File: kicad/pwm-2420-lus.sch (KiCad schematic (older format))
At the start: 6 parts

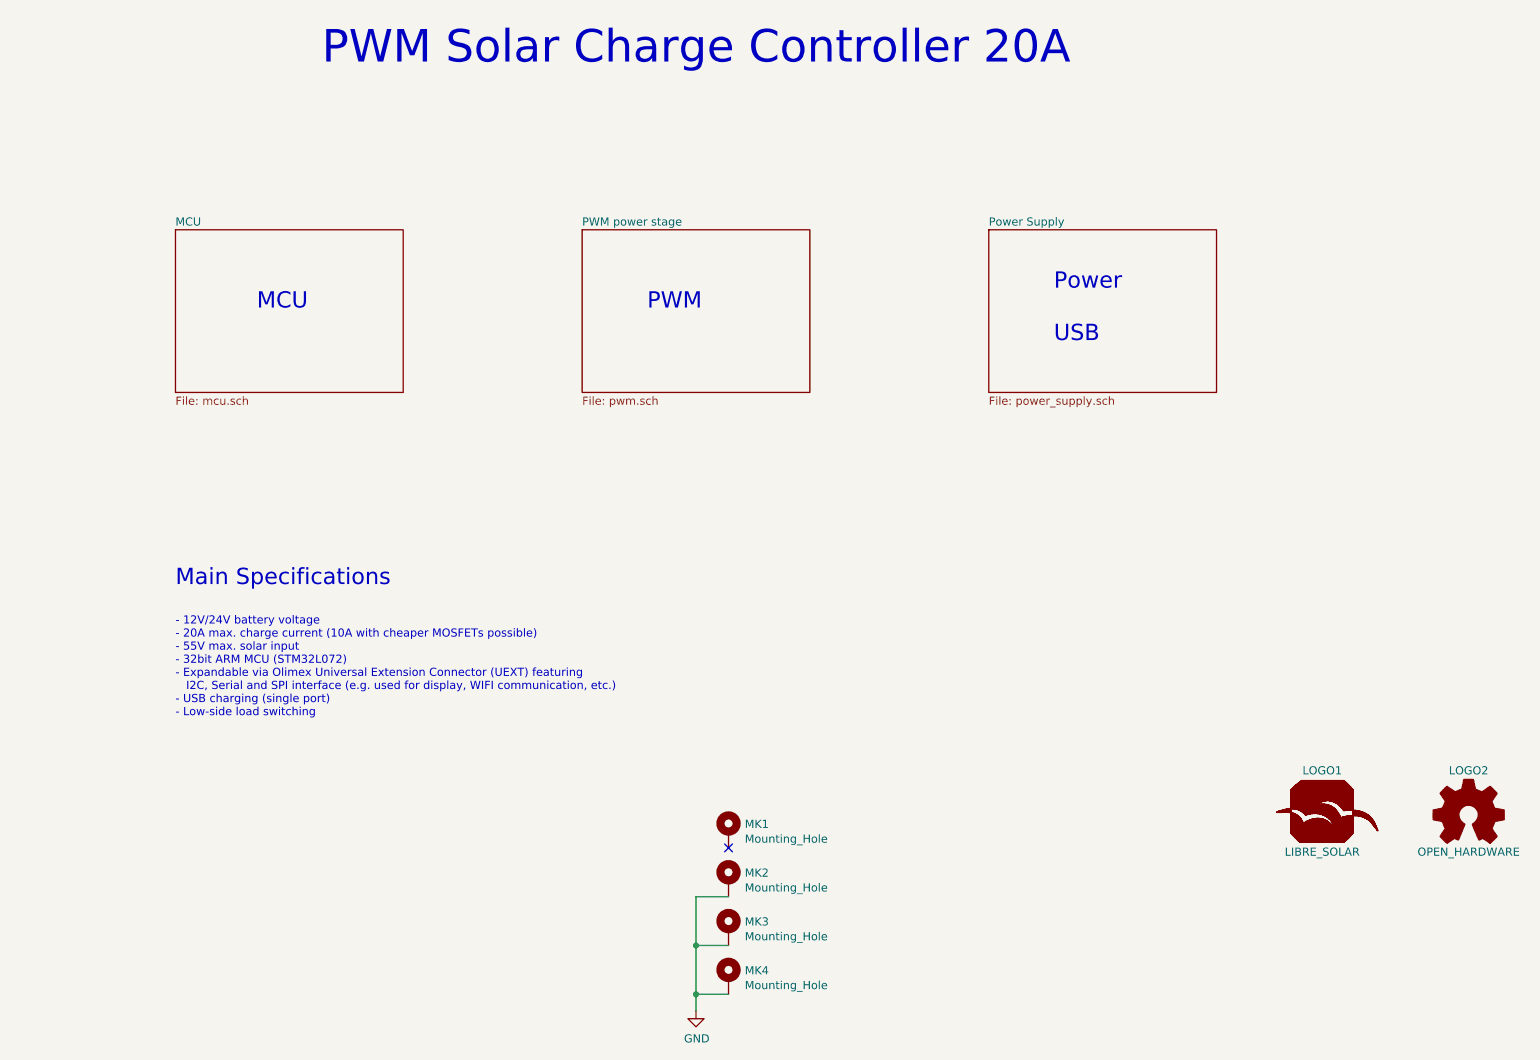
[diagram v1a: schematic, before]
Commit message: Improved power supply and exposed BOOT0 pin
- BOOT0 pin connected to BUTTON wire to allow firmware upgrade via LS.one port
- Additional emitter follower for 3V3 power supply to increase margin to 30V absolute max. rating of LDO in case of 24V battery
- Corners adjusted to match shape of MPPT 1210 HUS
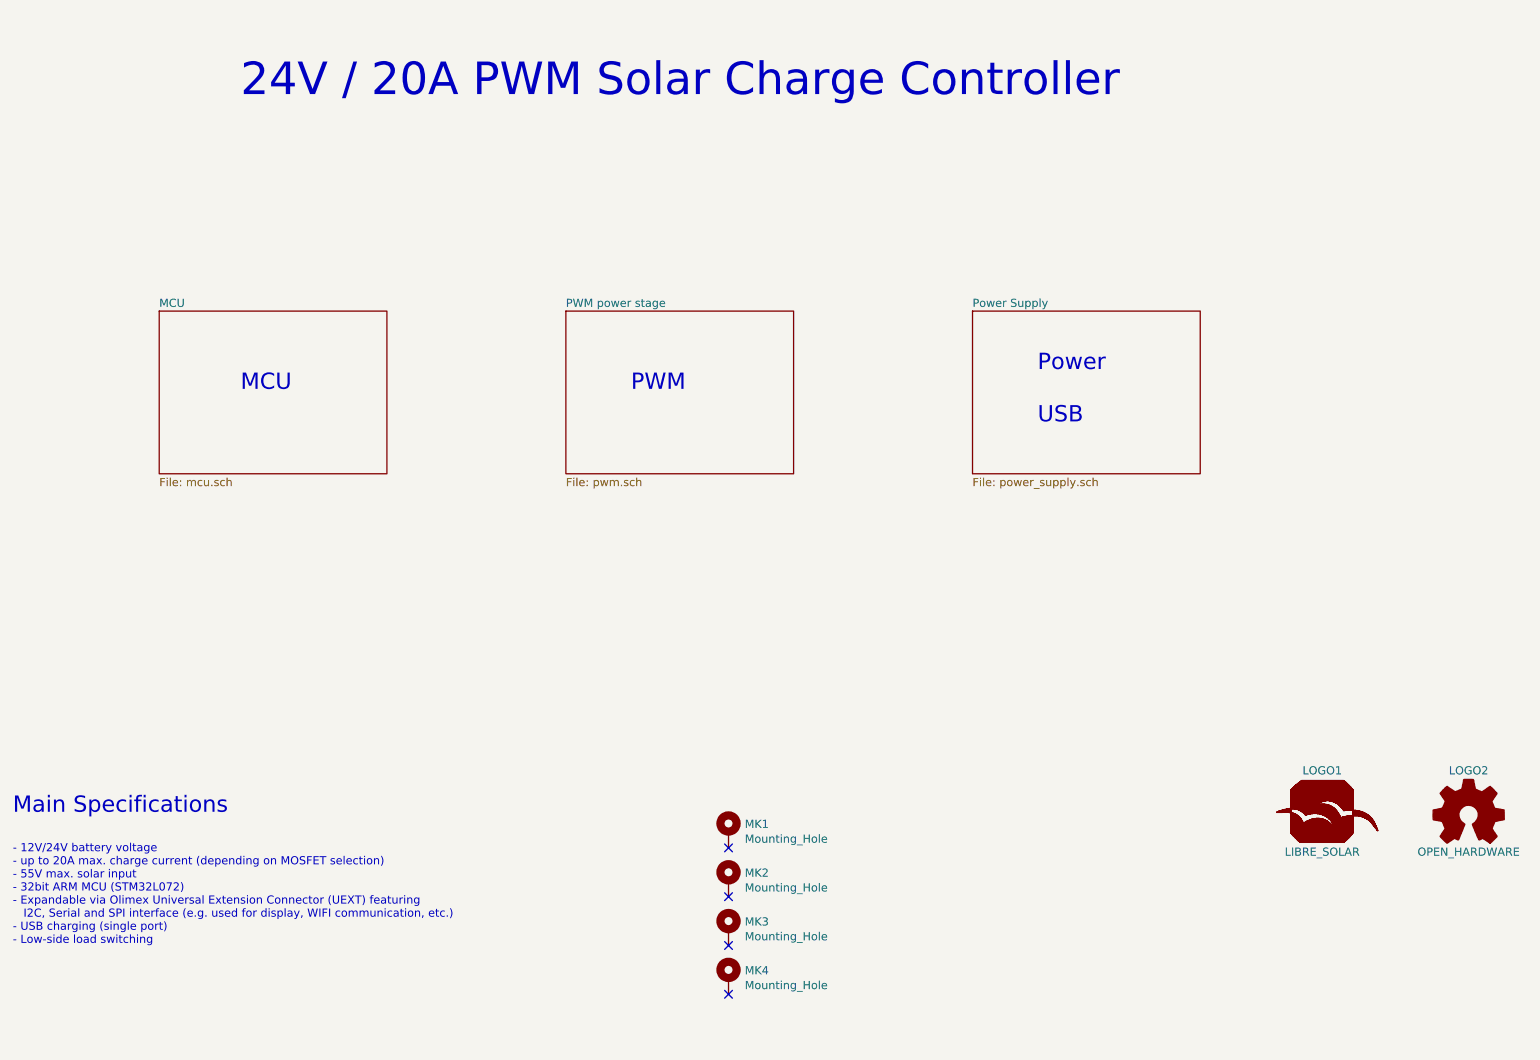
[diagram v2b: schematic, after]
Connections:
- removed net GND: MK2.1, MK3.1, MK4.1
- no-connect marks 1 -> 4
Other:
- note added: "- 12V/24V battery voltage\n- up to 20A max. charge current (depending on MOSFET selection)\n- 55V max. solar input\n- 32bit ARM MCU (STM32L072)\n- Expandable via Olimex Universal Extension Connector (UEXT) featuring\n I2C, Serial and SPI interface (e.g. used for display, WIFI communication, etc.)\n- USB charging (single port)\n- Low-side load switching\n"
- note added: "24V / 20A PWM Solar Charge Controller"
- note removed: "- 12V/24V battery voltage\n- 20A max. charge current (10A with cheaper MOSFETs possible)\n- 55V max. solar input\n- 32bit ARM MCU (STM32L072)\n- Expandable via Olimex Universal Extension Connector (UEXT) featuring\n I2C, Serial and SPI interface (e.g. used for display, WIFI communication, etc.)\n- USB charging (single port)\n- Low-side load switching\n"
- note removed: "PWM Solar Charge Controller 20A"
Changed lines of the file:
@@
 encoding utf-8
 Sheet 1 4
-Title "PWM Solar Charge Controller"
-Date "2019-04-25"
-Rev "0.2.2"
+Title "PWM 2420 LUS"
+Date "2019-08-26"
+Rev "0.3"
 Comp "Libre Solar"
 Comment1 "Author: Martin Jäger"
@@
 $EndDescr
 $Sheet
-S 5100 2500 1400 1000
+S 5000 3000 1400 1000
 U 58A68DC9
 F0 "PWM power stage" 50
@@
 $EndSheet
 $Sheet
-S 2600 2500 1400 1000
+S 2500 3000 1400 1000
 U 58A68DCB
 F0 "MCU" 50
@@
 $EndSheet
 $Sheet
-S 7600 2500 1400 1000
+S 7500 3000 1400 1000
 U 58C18D5C
 F0 "Power Supply" 50
 F1 "power_supply.sch" 50
 $EndSheet
-Text Notes 3500 1500 0    200  ~ 0
-PWM Solar Charge Controller 20A
-Text Notes 2600 4700 0    100  ~ 0
+Text Notes 3000 1700 0    200  ~ 0
+24V / 20A PWM Solar Charge Controller
+Text Notes 1600 6100 0    100  ~ 0
 Main Specifications
-Text Notes 2600 5500 0    50   ~ 0
-- 12V/24V battery voltage\n- 20A max. charge current (10A with cheaper MOSFETs possible)\n- 55V max. solar input\n- 32bit ARM MCU (STM32L072)\n- Expandable via Olimex Universal Extension Connector (UEXT) featuring\n   I2C, Serial and SPI interface (e.g. used for display, WIFI communication, etc.)\n- USB charging (single port)\n- Low-side load switching\n
+Text Notes 1600 6900 0    50   ~ 0
+- 12V/24V battery voltage\n- up to 20A max. charge current (depending on MOSFET selection)\n- 55V max. solar input\n- 32bit ARM MCU (STM32L072)\n- Expandable via Olimex Universal Extension Connector (UEXT) featuring\n   I2C, Serial and SPI interface (e.g. used for display, WIFI communication, etc.)\n- USB charging (single port)\n- Low-side load switching\n
 $Comp
 L Project:Logo_Open_Hardware_Small LOGO2
@@
 	1    0    0    -1
 $EndComp
-Text Notes 5500 3000 0    100  ~ 0
+Text Notes 5400 3500 0    100  ~ 0
 PWM
-Text Notes 3100 3000 0    100  ~ 0
+Text Notes 3000 3500 0    100  ~ 0
 MCU
-Text Notes 8000 3200 0    100  ~ 0
+Text Notes 7900 3700 0    100  ~ 0
 Power\n\nUSB
 $Comp
@@
 	1    0    0    -1
 $EndComp
-Wire Wire Line
-	5800 6600 6000 6600
-$Comp
-L power:GND #PWR0106
-U 1 1 5AF1E99A
-P 5800 7300
-F 0 "#PWR0106" H 5800 7050 50  0001 C CNN
-F 1 "GND" H 5805 7127 50  0000 C CNN
-F 2 "" H 5800 7300 50  0001 C CNN
-F 3 "" H 5800 7300 50  0001 C CNN
-	1    5800 7300
-	1    0    0    -1
-$EndComp
 $Comp
 L Mechanical:MountingHole_Pad MK4
@@
 	1    0    0    -1
 $EndComp
-Wire Wire Line
-	6000 7200 5800 7200
-Connection ~ 5800 7200
-Wire Wire Line
-	5800 7200 5800 7300
-Wire Wire Line
-	5800 6600 5800 6900
-Wire Wire Line
-	6000 6900 5800 6900
-Connection ~ 5800 6900
-Wire Wire Line
-	5800 6900 5800 7200
 NoConn ~ 6000 6300
+NoConn ~ 6000 6600
+NoConn ~ 6000 6900
+NoConn ~ 6000 7200
 $EndSCHEMATC
